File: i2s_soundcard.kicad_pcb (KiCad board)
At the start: 4 copper layers, 83.1 x 112.6 mm, 11 parts, among them J1 Conn_01x08, J2 Conn_01x06, U1 TLV320AIC3104IRHBT, U2 FSA2275UMX, U3 TPA2006D1DRBR, U4 FSA2275UMX, U5 TPA2006D1DRBR

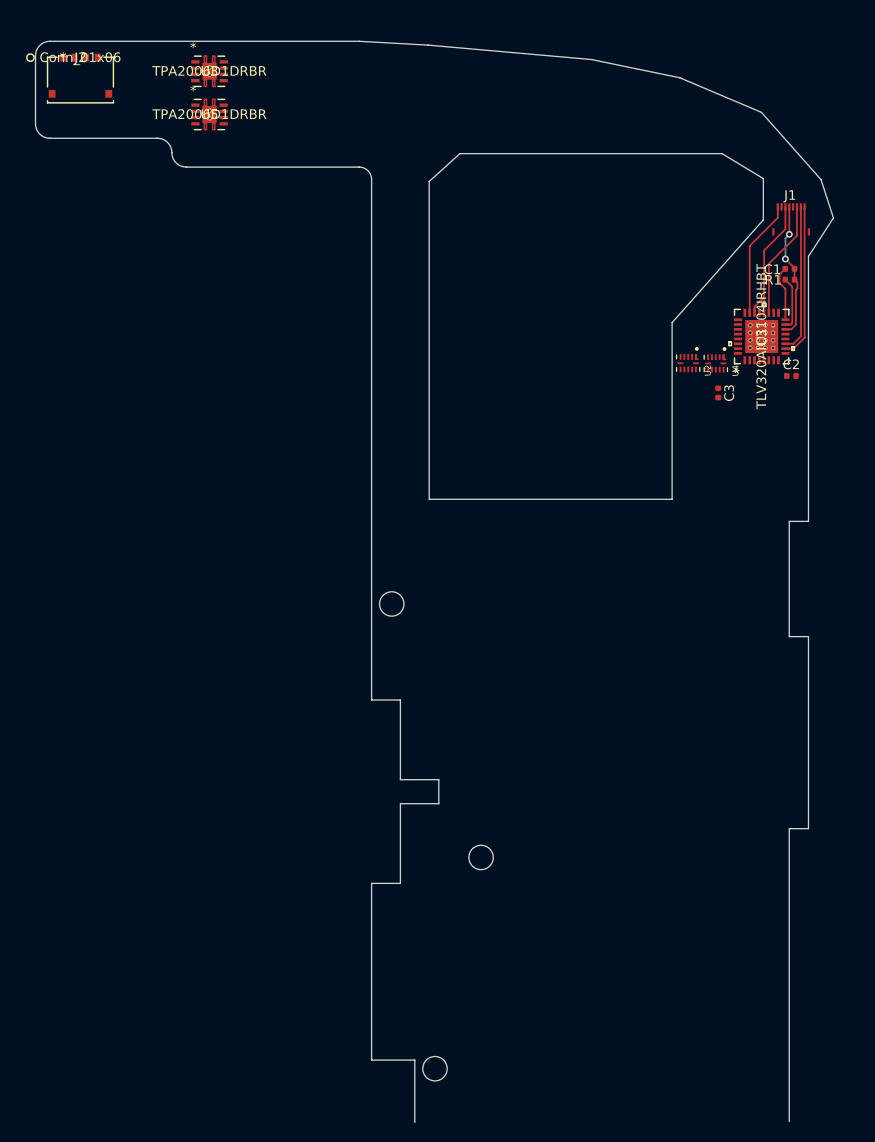
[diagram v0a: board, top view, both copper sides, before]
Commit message: Lots more routing; set V pads on TPA2006 to GND; add 1.8V/3.3V dual LDO: TLV7111830. Save datasheets to project directory for safe keeping.
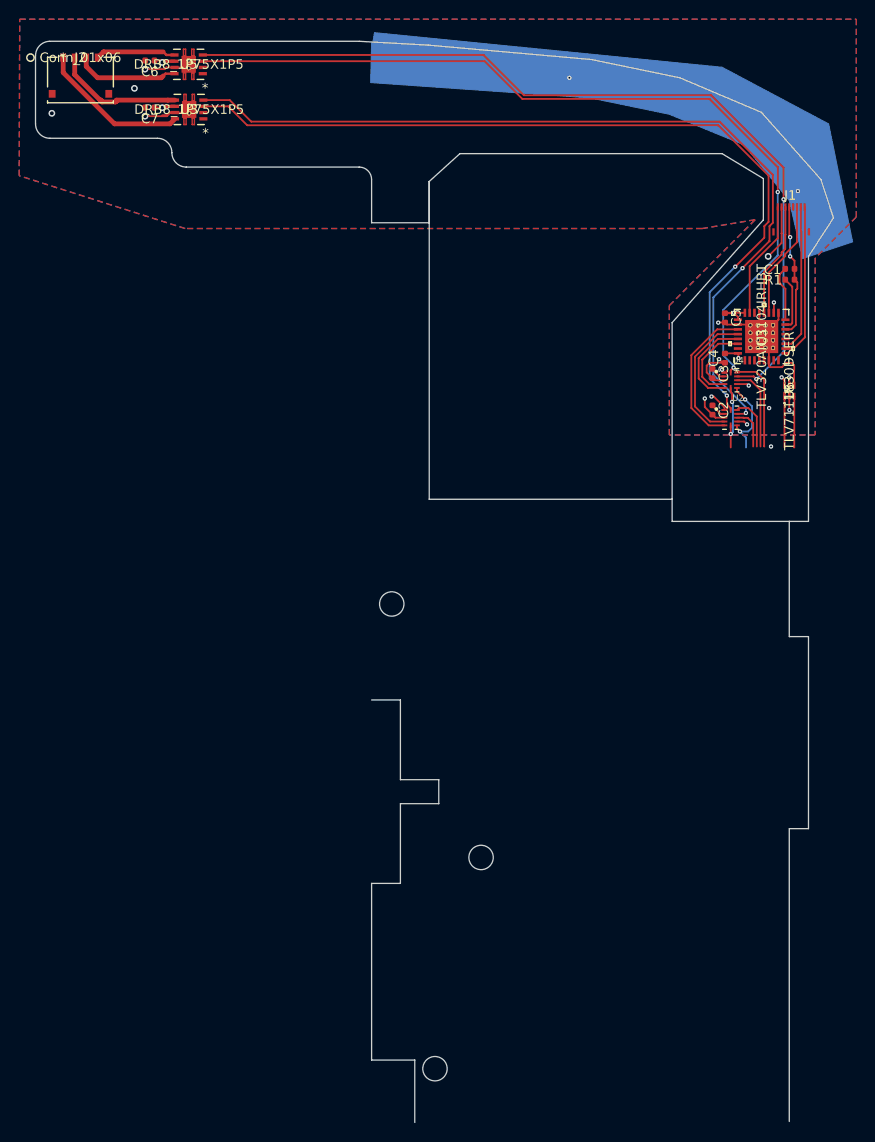
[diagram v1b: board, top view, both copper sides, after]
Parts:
- added C4: 1uF, Capacitor_SMD:C_0402_1005Metric, F.Cu at (159.6, 91.3)
- added C5: 1uF, Capacitor_SMD:C_0402_1005Metric, F.Cu at (159.6, 87.1)
- added C6: 1uF, Capacitor_SMD:C_0402_1005Metric, F.Cu at (99.7, 60.3)
- added C7: 1uF, Capacitor_SMD:C_0402_1005Metric, F.Cu at (99.7, 65.2)
- added U6: TLV7111830DSER, footprints:TLV7111830DSER, F.Cu at (166.3, 94.7)
- C2, C3: value C -> 0.1uF
- U3, U5: value TPA2006D1DRBR -> DRB8_1P75X1P5
- moved C2 8.96 mm to (158.3, 96.7), turned to 270 degrees
- moved U2 7.20 mm to (160.2, 97.5), turned to 0 degrees
- moved U5 5.66 mm to (103.8, 60.7), turned to 180 degrees
- moved U3 4.51 mm to (103.8, 65.4), turned to 180 degrees
- moved U4 2.34 mm to (160.2, 93.6), turned to 0 degrees
- moved C3 2.11 mm to (158.3, 92.9)
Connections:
- net /spkr_amp_left/VDD renamed /vbat
- net Net-(U2-Pad10) renamed /spkr_amp_left/SLO-
- net Net-(U2-Pad12) renamed /spkr_amp_left/SLO+
- net Net-(U4-Pad10) renamed /spkr_amp_right/SLO-
- net Net-(U4-Pad12) renamed /spkr_amp_right/SLO+
- U1 pad 17: Net-(U1-Pad17) -> GND
- U1 pad 18: Net-(U1-Pad18) -> /v3.3
- U1 pad 21: Net-(U1-Pad21) -> GND
- U1 pad 24: Net-(U1-Pad24) -> /v3.3
- U1 pad 25: Net-(U1-Pad25) -> /v3.3
- U1 pad 26: Net-(U1-Pad26) -> GND
- U1 pad 32: Net-(U1-Pad32) -> /v1.8
- U1 pad 6: Net-(U1-Pad6) -> GND
- U2 pad 11: /spkr_amp_left/LINEOUT+ -> /spkr_amp_left/LINEOUT-
- U2 pad 4: /spkr_amp_left/LINEIN+ -> /spkr_amp_left/LINEIN-
- U2 pad 5: /spkr_amp_left/LINEIN- -> /spkr_amp_left/LINEIN+
- U2 pad 9: /spkr_amp_left/LINEOUT- -> /spkr_amp_left/LINEOUT+
- U3 pad 5: /spkr_amp_left/SPKR+ -> /spkr_amp_left/SPKR-
- U3 pad 8: /spkr_amp_left/SPKR- -> /spkr_amp_left/SPKR+
- U4 pad 11: /spkr_amp_right/LINEOUT+ -> /spkr_amp_right/LINEOUT-
- U4 pad 4: /spkr_amp_right/LINEIN+ -> /spkr_amp_right/LINEIN-
- U4 pad 5: /spkr_amp_right/LINEIN- -> /spkr_amp_right/LINEIN+
- U4 pad 9: /spkr_amp_right/LINEOUT- -> /spkr_amp_right/LINEOUT+
- U5 pad 5: /spkr_amp_right/SPKR+ -> /spkr_amp_right/SPKR-
- U5 pad 8: /spkr_amp_right/SPKR- -> /spkr_amp_right/SPKR+
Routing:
- net /spkr_amp_left/SLO-: track 0.00 -> 92.3 mm, vias 0 -> 2
- net /spkr_amp_right/SLO-: track 0.00 -> 90.7 mm, vias 0 -> 2
- net /spkr_amp_left/SLO+: track 0.00 -> 89.7 mm, vias 0 -> 2
- net /spkr_amp_right/SLO+: track 0.00 -> 88.8 mm, vias 0 -> 2
- net GND: track 0.00 -> 42.2 mm, vias 0 -> 12
- net /vbat: track 0.00 -> 29.4 mm, vias 0 -> 6
- net /v3.3: track 0.00 -> 19.8 mm, vias 0 -> 3
- net /spkr_amp_left/LINEIN+: track 0.00 -> 15.7 mm
- net /spkr_amp_left/SPKR+: track 0.00 -> 15.6 mm
- net /spkr_amp_left/LINEIN-: track 0.00 -> 14.3 mm
- net /spkr_amp_left/SPKR-: track 0.00 -> 13.6 mm
- net /spkr_amp_right/SPKR+: track 0.00 -> 10.8 mm
- net /spkr_amp_right/LINEOUT-: track 0.00 -> 10.2 mm
- net /spkr_amp_right/LINEIN+: track 0.00 -> 10.1 mm
- net /spkr_amp_left/MUTE: track 0.00 -> 8.91 mm, vias 0 -> 2
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- added copper zone on In2.Cu, net /vbat
- added copper zone on B.Cu, net GND
- added copper zone on F.Cu, net GND
- added copper zone on In1.Cu, net GND
- added copper zone on In2.Cu, net GND
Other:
- outline, holes or cut-outs redrawn

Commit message: Break out more nets to pins, move switches down to make room for those traces. Reroute a lot of things.
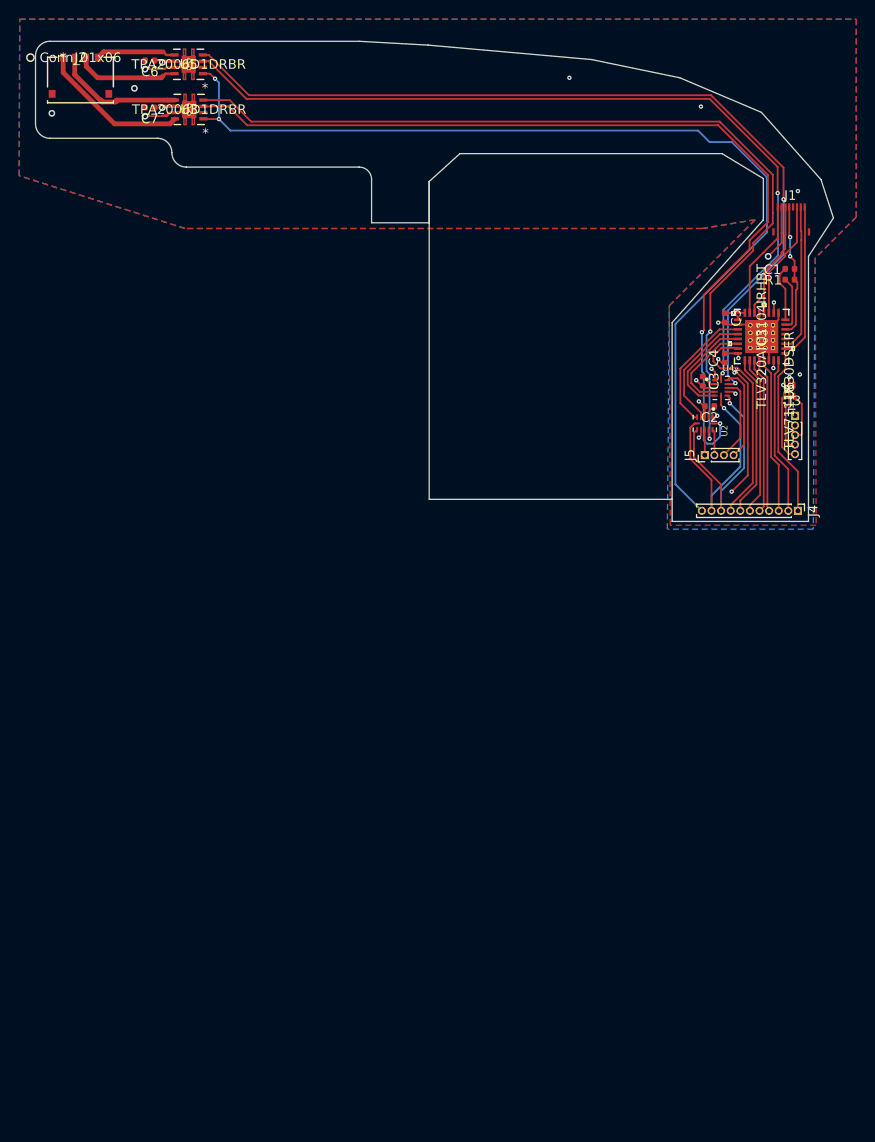
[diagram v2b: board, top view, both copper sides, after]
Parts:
- added J3: Conn_01x05, Connector_PinHeader_1.00mm:PinHeader_1x05_P1.00mm_Vertical, F.Cu at (166.9, 97.3)
- added J4: Conn_01x11, Connector_PinHeader_1.00mm:PinHeader_1x11_P1.00mm_Vertical, F.Cu at (167.2, 107.2)
- added J5: Conn_01x04, Connector_PinHeader_1.00mm:PinHeader_1x04_P1.00mm_Vertical, F.Cu at (157.5, 101.4)
- U3, U5: value DRB8_1P75X1P5 -> TPA2006D1DRBR
- moved U2 2.77 mm to (157.5, 98.1), turned to 270 degrees
- moved U4 1.28 mm to (159.2, 94.4)
- moved C3 1.28 mm to (157.3, 93.7)
- moved C2 0.50 mm to (158.0, 96.3), turned to 180 degrees
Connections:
- net /spkr_amp_left/MUTE renamed /mute
- net /spkr_amp_left/SEL renamed /sel
- net /spkr_amp_left/~SHUTDOWN renamed /~shutdown
- U1 pad 1: Net-(U1-Pad1) -> /mclk
- U1 pad 2: Net-(U1-Pad2) -> /bclk
- U1 pad 3: Net-(U1-Pad3) -> /wclk
- U1 pad 31: Net-(U1-Pad31) -> /reset
- U1 pad 4: Net-(U1-Pad4) -> /din
- U1 pad 5: Net-(U1-Pad5) -> /dout
- U1 pad 7: Net-(U1-Pad7) -> /iovdd
- U1 pad 8: Net-(U1-Pad8) -> /scl
- U1 pad 9: Net-(U1-Pad9) -> /sca
- U2 pad 11: /spkr_amp_left/LINEOUT- -> /LOR-
- U2 pad 9: /spkr_amp_left/LINEOUT+ -> /LOR+
- U4 pad 11: /spkr_amp_right/LINEOUT- -> /LOL-
- U4 pad 9: /spkr_amp_right/LINEOUT+ -> /LOL+
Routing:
- net /~shutdown: track 0.00 -> 106.9 mm, vias 0 -> 2
- net /reset: track 0.00 -> 22.8 mm
- net /sca: track 0.00 -> 17.6 mm
- net /sel: track 7.29 -> 24.5 mm, vias 2 -> 1
- net /mclk: track 0.00 -> 16.9 mm
- net /bclk: track 0.00 -> 16.6 mm
- net /scl: track 0.00 -> 16.4 mm
- net /dout: track 0.00 -> 16.3 mm
- net /wclk: track 0.00 -> 16.3 mm
- net /din: track 0.00 -> 16.1 mm
- net /mute: track 8.91 -> 23.6 mm, vias 2 -> 1
- net /spkr_amp_right/LINEOUT-: track 10.2 -> 0.00 mm
- net /LOL-: track 0.00 -> 9.89 mm
- net /LOL+: track 0.00 -> 8.86 mm
- net /spkr_amp_right/LINEOUT+: track 8.75 -> 0.00 mm
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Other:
- board size 83.1 x 112.6 mm -> 83.1 x 50 mm

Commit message: Tweak ground planes a bit.
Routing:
- net GND: vias 16 -> 20
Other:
- outline, holes or cut-outs redrawn
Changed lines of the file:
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@@
   (general
     (thickness 1)
-    (drawings 43)
-    (tracks 420)
+    (drawings 41)
+    (tracks 424)
     (zones 0)
     (modules 19)
@@
   (gr_line (start 166.3 108.3) (end 154.1 108.3) (layer Edge.Cuts) (width 0.12))
   (gr_line (start 122.8 77.2) (end 128.8 77.2) (layer Edge.Cuts) (width 0.12))
-  (gr_line (start 128.8 106) (end 154.1 106) (layer Edge.Cuts) (width 0.12))
   (gr_line (start 163.6 72.6) (end 163.6 76.9) (layer Edge.Cuts) (width 0.12))
   (gr_line (start 163.6 76.9) (end 154.1 87.6) (layer Edge.Cuts) (width 0.12))
@@
   (gr_line (start 159.3 70) (end 132 70) (layer Edge.Cuts) (width 0.12))
   (gr_line (start 132 70) (end 128.8 72.9) (layer Edge.Cuts) (width 0.12))
-  (gr_line (start 128.8 106) (end 128.8 72.9) (layer Edge.Cuts) (width 0.12))
   (gr_text "Round these corners! 1mm radius\n" (at 119 153 90) (layer Cmts.User)
     (effects (font (size 2 2) (thickness 0.15)))
@@
   (via (at 99.2 61.2) (size 0.7) (drill 0.4) (layers F.Cu B.Cu) (net 3))
   (segment (start 99.2 60.315) (end 99.215 60.3) (width 0.19) (layer F.Cu) (net 3))
-  (via (at 143.4 62.1) (size 0.45) (drill 0.2) (layers F.Cu B.Cu) (net 3))
-  (via (at 167.2 73.9) (size 0.45) (drill 0.2) (layers F.Cu B.Cu) (net 3))
+  (via (at 166.2 73.8) (size 0.45) (drill 0.2) (layers F.Cu B.Cu) (net 3))
   (segment (start 159.6 87.585) (end 158.915021 87.585) (width 0.19) (layer F.Cu) (net 3))
   (via (at 158.900021 87.6) (size 0.45) (drill 0.2) (layers F.Cu B.Cu) (net 3))
   (segment (start 158.915021 87.585) (end 158.900021 87.6) (width 0.19) (layer F.Cu) (net 3))
-  (via (at 157.1 65.1) (size 0.45) (drill 0.2) (layers F.Cu B.Cu) (net 3))
   (via (at 167.4 93) (size 0.45) (drill 0.2) (layers F.Cu B.Cu) (net 3))
   (segment (start 157.5 96.315) (end 157.515 96.3) (width 0.19) (layer F.Cu) (net 3))
@@
   (via (at 156.610013 93.6) (size 0.45) (drill 0.2) (layers F.Cu B.Cu) (net 3))
   (segment (start 157.195013 94.185) (end 156.610013 93.6) (width 0.19) (layer F.Cu) (net 3))
+  (via (at 164.4 71.2) (size 0.45) (drill 0.2) (layers F.Cu B.Cu) (net 3))
+  (via (at 136 65.8) (size 0.45) (drill 0.2) (layers F.Cu B.Cu) (net 3))
+  (via (at 135.9 63.2) (size 0.45) (drill 0.2) (layers F.Cu B.Cu) (net 3))
+  (via (at 136 68.5) (size 0.45) (drill 0.2) (layers F.Cu B.Cu) (net 3))
+  (via (at 158.4 65.9) (size 0.45) (drill 0.2) (layers F.Cu B.Cu) (net 3))
+  (via (at 160.8 70.1) (size 0.45) (drill 0.2) (layers F.Cu B.Cu) (net 3))
   (segment (start 157.9 96.885) (end 158.485 96.3) (width 0.19) (layer F.Cu) (net 4))
   (segment (start 157.9 97.45) (end 157.9 96.885) (width 0.19) (layer F.Cu) (net 4))
@@
   (segment (start 158.344801 100.210001) (end 157.755199 100.210001) (width 0.19) (layer B.Cu) (net 27))
   (segment (start 159.1 99.454802) (end 158.344801 100.210001) (width 0.19) (layer B.Cu) (net 27))
-  (segment (start 158.157406 63.91999) (end 165.7 71.462584) (width 0.19) (layer F.Cu) (net 28))
-  (segment (start 165.7 71.462584) (end 165.7 74.270195) (width 0.19) (layer F.Cu) (net 28))
-  (segment (start 105.840001 59.725001) (end 110.03499 63.91999) (width 0.19) (layer F.Cu) (net 28))
-  (segment (start 110.03499 63.91999) (end 158.157406 63.91999) (width 0.19) (layer F.Cu) (net 28))
-  (segment (start 165.7 74.270195) (end 165.7 74.759978) (width 0.19) (layer F.Cu) (net 28))
-  (segment (start 105.225001 59.725001) (end 105.840001 59.725001) (width 0.19) (layer F.Cu) (net 28))
   (via (at 165.7 74.759978) (size 0.45) (drill 0.2) (layers F.Cu B.Cu) (net 28))
   (segment (start 159.85 94) (end 160.600008 94) (width 0.19) (layer F.Cu) (net 28))
@@
   (segment (start 165.7 80.537414) (end 159.9 86.337416) (width 0.19) (layer B.Cu) (net 28))
   (segment (start 159.9 86.337416) (end 159.9 93.11257) (width 0.19) (layer B.Cu) (net 28))
-  (segment (start 165.090013 71.390013) (end 165.090013 74.109987) (width 0.19) (layer F.Cu) (net 29))
-  (segment (start 105.840001 60.374999) (end 109.765002 64.3) (width 0.19) (layer F.Cu) (net 29))
-  (segment (start 109.765002 64.3) (end 158 64.3) (width 0.19) (layer F.Cu) (net 29))
-  (segment (start 158 64.3) (end 165.090013 71.390013) (width 0.19) (layer F.Cu) (net 29))
-  (segment (start 105.225001 60.374999) (end 105.840001 60.374999) (width 0.19) (layer F.Cu) (net 29))
+  (segment (start 110.83499 64.71999) (end 159.357406 64.71999) (width 0.19) (layer F.Cu) (net 28))
+  (segment (start 105.225001 59.725001) (end 105.840001 59.725001) (width 0.19) (layer F.Cu) (net 28))
+  (segment (start 105.840001 59.725001) (end 110.83499 64.71999) (width 0.19) (layer F.Cu) (net 28))
+  (segment (start 165.7 71.062584) (end 165.7 74.44178) (width 0.19) (layer F.Cu) (net 28))
+  (segment (start 159.357406 64.71999) (end 165.7 71.062584) (width 0.19) (layer F.Cu) (net 28))
+  (segment (start 165.7 74.44178) (end 165.7 74.759978) (width 0.19) (layer F.Cu) (net 28))
   (via (at 165.090013 74.109987) (size 0.45) (drill 0.2) (layers F.Cu B.Cu) (net 29))
   (segment (start 159.2 93.032867) (end 159.357847 92.87502) (width 0.19) (layer F.Cu) (net 29))
@@
   (segment (start 165.124999 74.144973) (end 165.124999 80.575001) (width 0.19) (layer B.Cu) (net 29))
   (segment (start 159.434094 86.265906) (end 159.434094 92.798773) (width 0.19) (layer B.Cu) (net 29))
+  (segment (start 165.090013 70.990013) (end 165.090013 74.109987) (width 0.19) (layer F.Cu) (net 29))
+  (segment (start 110.565002 65.1) (end 159.2 65.1) (width 0.19) (layer F.Cu) (net 29))
+  (segment (start 105.840001 60.374999) (end 110.565002 65.1) (width 0.19) (layer F.Cu) (net 29))
+  (segment (start 159.2 65.1) (end 165.090013 70.990013) (width 0.19) (layer F.Cu) (net 29))
+  (segment (start 105.225001 60.374999) (end 105.840001 60.374999) (width 0.19) (layer F.Cu) (net 29))
   (segment (start 159.614559 90.800441) (end 159.6 90.815) (width 0.19) (layer F.Cu) (net 30))
   (segment (start 160.950001 90.800441) (end 159.614559 90.800441) (width 0.19) (layer F.Cu) (net 30))
@@
       (pts
         (xy 173.275 76.6) (xy 169 80.875) (xy 168.5 106.9) (xy 164.5 106.2) (xy 164.3375 94.7375)
-        (xy 166.6 81.2) (xy 166.6 73) (xy 156.198438 72.959375) (xy 103.3875 77.8) (xy 86.1 72.3)
-        (xy 86.15 56) (xy 173.275 56)
+        (xy 166.4 81.2) (xy 168 73.2) (xy 164.4 70.1) (xy 163 73.1) (xy 103.3875 77.8)
+        (xy 86.1 72.3) (xy 86.15 56) (xy 173.275 56)
       )
     )
@@
     (polygon
       (pts
-        (xy 166.3 74.6) (xy 166.3 80.9) (xy 160.2 87) (xy 160.2 90.7) (xy 163 93.5)
-        (xy 163 98.5) (xy 159.5 98.5) (xy 159.5 95.9) (xy 157.7 94.1) (xy 157.7 73.2)
-        (xy 164.9 73.2)
+        (xy 164.4 70.5) (xy 167.8 73.4) (xy 166.3 80.9) (xy 160.2 87) (xy 160.2 90.7)
+        (xy 161.3 93.6) (xy 161.3 95.4) (xy 159.35 95.4) (xy 159.5 95.9) (xy 157.7 94.1)
+        (xy 158.9 85.8) (xy 164.3 80.3) (xy 163.4 73)
       )
     )

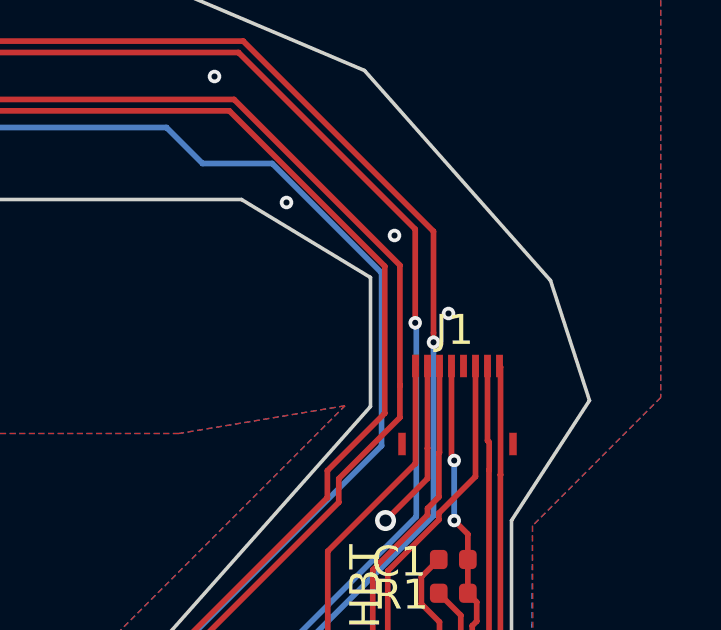
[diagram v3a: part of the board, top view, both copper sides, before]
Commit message: Drop clearance requirements and move vias/ground planes around to make DRC happy.
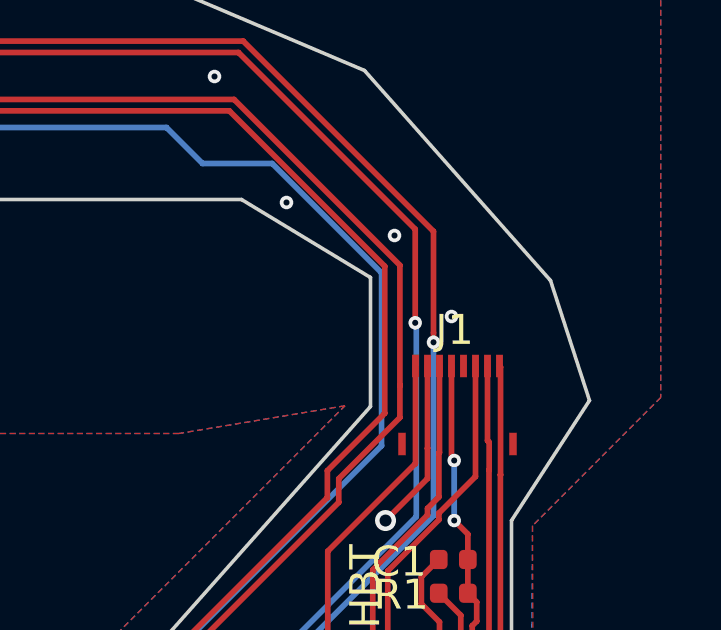
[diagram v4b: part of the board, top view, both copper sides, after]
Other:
- net class Default: clearance 0.19 -> 0.15
- rule trace_clearance: 0.19 -> 0.15
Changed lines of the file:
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@@
     (33 F.Adhes user)
     (34 B.Paste user)
-    (35 F.Paste user)
+    (35 F.Paste user hide)
     (36 B.SilkS user hide)
     (37 F.SilkS user hide)
@@
     (user_trace_width 0.254)
     (user_trace_width 0.5)
-    (trace_clearance 0.19)
+    (trace_clearance 0.15)
     (zone_clearance 0.127)
     (zone_45_only no)
@@
   (net 50 /~shutdown)
   (net_class Default "This is the default net class."
-    (clearance 0.19)
+    (clearance 0.15)
     (trace_width 0.19)
     (via_dia 0.7)
@@
   (via (at 99.2 61.2) (size 0.7) (drill 0.4) (layers F.Cu B.Cu) (net 3))
   (segment (start 99.2 60.315) (end 99.215 60.3) (width 0.19) (layer F.Cu) (net 3))
-  (via (at 166.2 73.8) (size 0.45) (drill 0.2) (layers F.Cu B.Cu) (net 3))
+  (via (at 166.3 73.9) (size 0.45) (drill 0.2) (layers F.Cu B.Cu) (net 3))
   (segment (start 159.6 87.585) (end 158.915021 87.585) (width 0.19) (layer F.Cu) (net 3))
   (via (at 158.900021 87.6) (size 0.45) (drill 0.2) (layers F.Cu B.Cu) (net 3))
@@
       (pts
         (xy 173.275 76.6) (xy 169 80.875) (xy 168.5 106.9) (xy 164.5 106.2) (xy 164.3375 94.7375)
-        (xy 166.4 81.2) (xy 168 73.2) (xy 164.4 70.1) (xy 163 73.1) (xy 103.3875 77.8)
+        (xy 166.4 81.2) (xy 168 73.2) (xy 164.3 70.1) (xy 163 73.1) (xy 103.3875 77.8)
         (xy 86.1 72.3) (xy 86.15 56) (xy 173.275 56)
       )
@@
     (polygon
       (pts
-        (xy 164.4 70.5) (xy 167.8 73.4) (xy 166.3 80.9) (xy 160.2 87) (xy 160.2 90.7)
+        (xy 164.4 70.5) (xy 167.7 73.3) (xy 166.3 80.9) (xy 160.2 87) (xy 160.2 90.7)
         (xy 161.3 93.6) (xy 161.3 95.4) (xy 159.35 95.4) (xy 159.5 95.9) (xy 157.7 94.1)
         (xy 158.9 85.8) (xy 164.3 80.3) (xy 163.4 73)
